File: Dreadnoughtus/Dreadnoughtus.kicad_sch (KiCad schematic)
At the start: 382 parts, among them U1 Elite-C, U2 PRTR5V0U2X, U3 PRTR5V0U2X

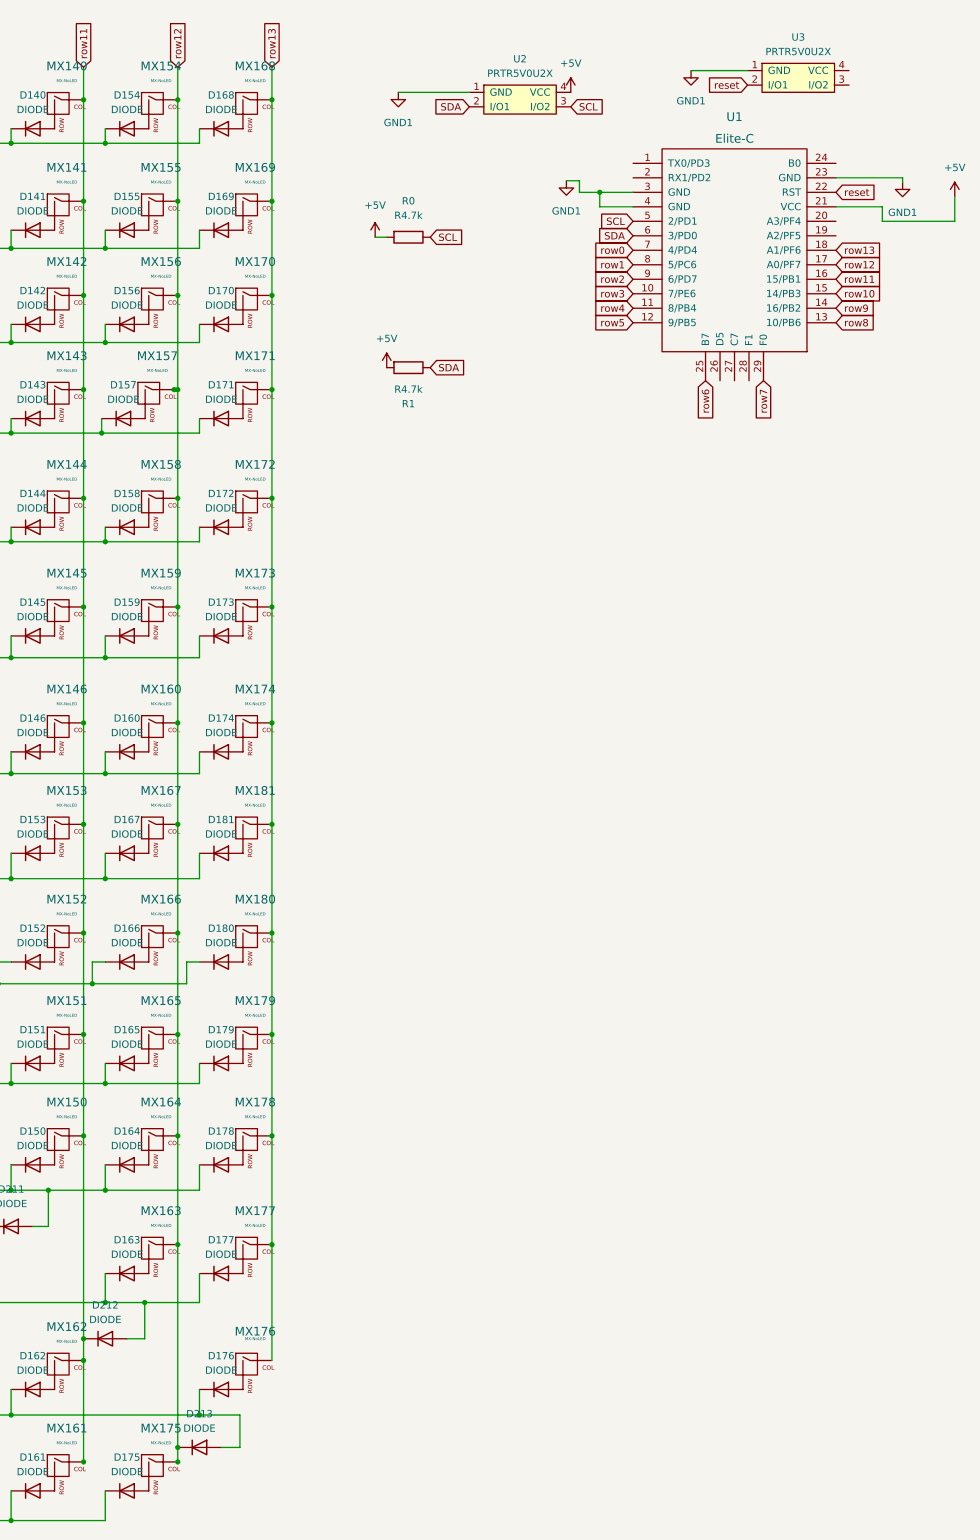
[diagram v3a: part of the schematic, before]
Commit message: tracked most switches and diodes
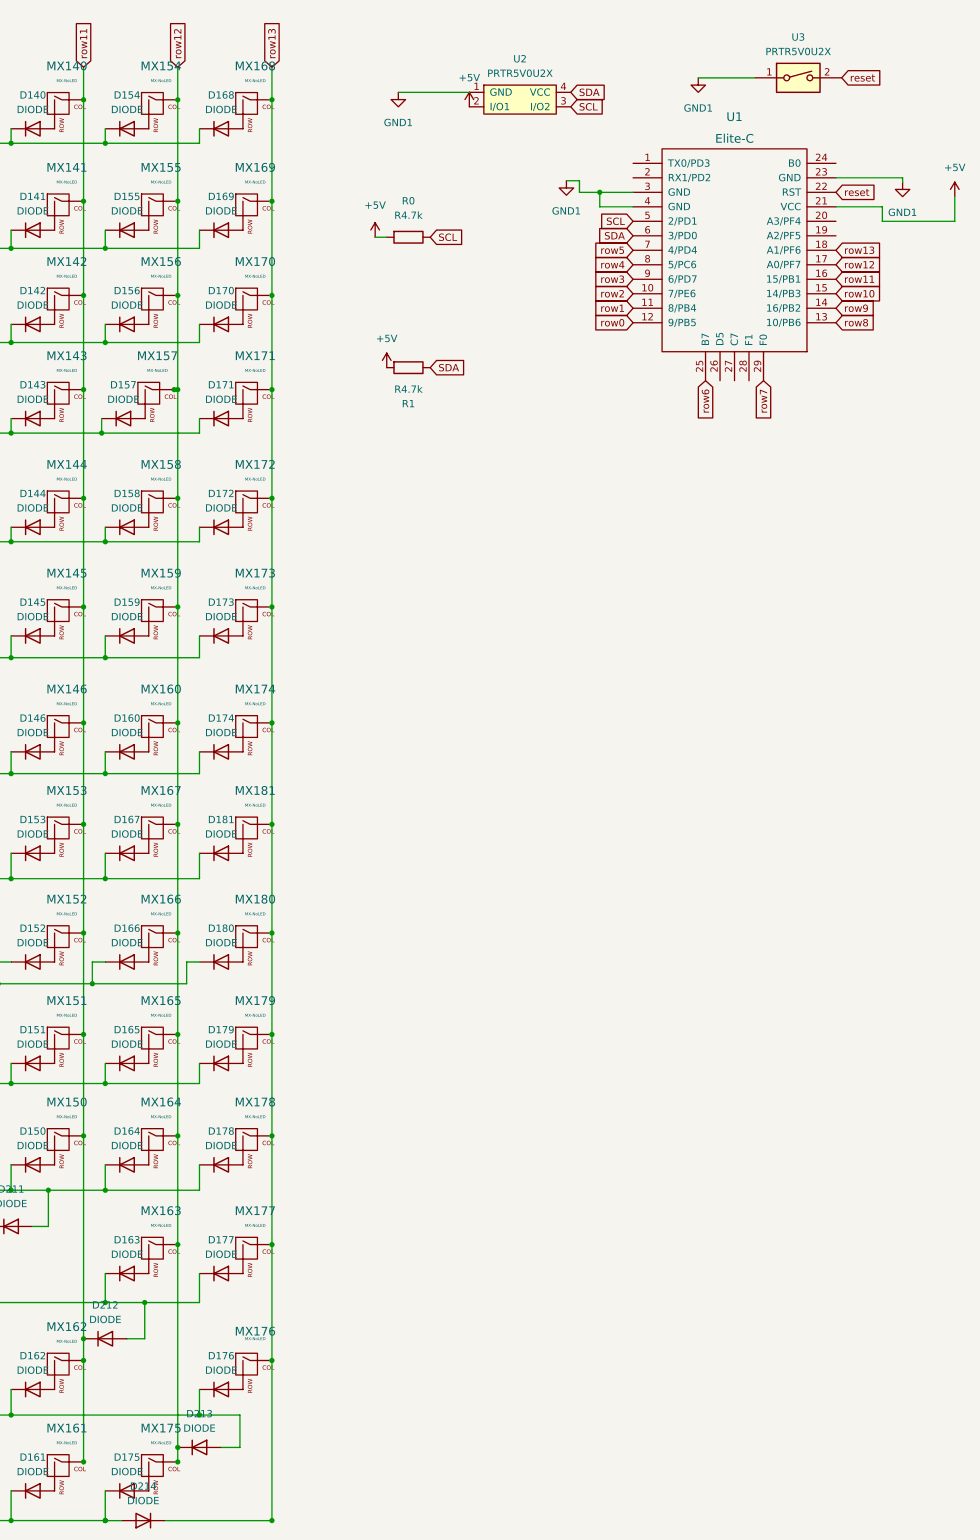
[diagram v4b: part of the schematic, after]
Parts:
- added D214: DIODE, Keebio-Parts:Diode-dual, symbol Simulation_SPICE:DIODE
- U1: footprint Keebio-Parts:Elite-C-castellated-29pin-holes -> Keebio-Parts:Elite-C
- U3: footprint Keebio-Parts:I2C_Breakout -> Keebio-Parts:SW_Tactile_SPST_Angled_MJTP1117; symbol keebio:PRTR5V0U2X -> Switch:SW_DIP_x01
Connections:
- net +5V: now also U2.2 (I/O1); no longer U2.4 (VCC)
- net SDA: now also U2.4 (VCC); no longer U2.2 (I/O1)
- net row0: now also U1.12 (9/PB5); no longer U1.7 (4/PD4)
- net row1: now also U1.11 (8/PB4); no longer U1.8 (5/PC6)
- net row13: now also D214.2 (K)
- net row2: now also U1.10 (7/PE6); no longer U1.9 (6/PD7)
- net row3: now also U1.9 (6/PD7); no longer U1.10 (7/PE6)
- net row4: now also U1.8 (5/PC6); no longer U1.11 (8/PB4)
- net row5: now also U1.7 (4/PD4); no longer U1.12 (9/PB5)
- net at D105.2 (K), D119.2 (K), D133.2 (K)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: now also D214.1 (A)

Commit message: rev 0 push, first completion
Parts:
- MX0, MX1, MX10, MX100, MX101, MX102, MX103, MX104, MX105, MX106, MX107, MX108, MX109, MX11, MX110, MX111, MX112, MX113, MX114, MX115, MX116, MX117, MX118, MX119, MX12, MX120, MX121, MX122, MX123, MX124, MX125, MX126, MX127, MX128, MX129, MX13, MX130, MX131, MX132, MX133, MX134, MX135, MX136, MX137, MX138, MX139, MX14, MX140, MX141, MX142, MX143, MX144, MX145, MX146, MX147, MX148, MX149, MX15, MX150, MX151, MX152, MX153, MX154, MX155, MX156, MX157, MX158, MX159, MX16, MX160, MX161, MX162, MX163, MX164, MX165, MX166, MX167, MX168, MX169, MX17, MX170, MX171, MX172, MX173, MX174, MX175, MX176, MX177, MX178, MX179, MX18, MX180, MX181, MX19, MX2, MX20, MX21, MX22, MX23, MX24, MX25, MX26, MX27, MX28, MX29, MX3, MX30, MX31, MX32, MX33, MX34, MX35, MX36, MX37, MX38, MX39, MX4, MX40, MX41, MX42, MX43, MX44, MX45, MX46, MX47, MX48, MX49, MX5, MX50, MX51, MX52, MX53, MX54, MX55, MX56, MX57, MX58, MX59, MX6, MX60, MX61, MX62, MX63, MX64, MX65, MX66, MX67, MX68, MX69, MX7, MX70, MX71, MX72, MX73, MX74, MX75, MX76, MX77, MX78, MX79, MX8, MX80, MX81, MX82, MX83, MX84, MX85, MX86, MX87, MX88, MX89, MX9, MX90, MX91, MX92, MX93, MX94, MX95, MX96, MX97, MX98, MX99: footprint MX_Alps_Hybrid:MXOnly-1U-Hotswap -> MX_Only:MXOnly-1U-Hotswap
